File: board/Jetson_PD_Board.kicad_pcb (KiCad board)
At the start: 2 copper layers, 47 parts, among them J1 USB4081-03-A, J2 768250002, Q1 NTTFS5C673NLTAG, Q2 NTTFS5C673NLTAG, Q3 NTTFS5C673NLTAG, U1 APK43070DKZ-13-FA01, U2 USBLC6-2SC6

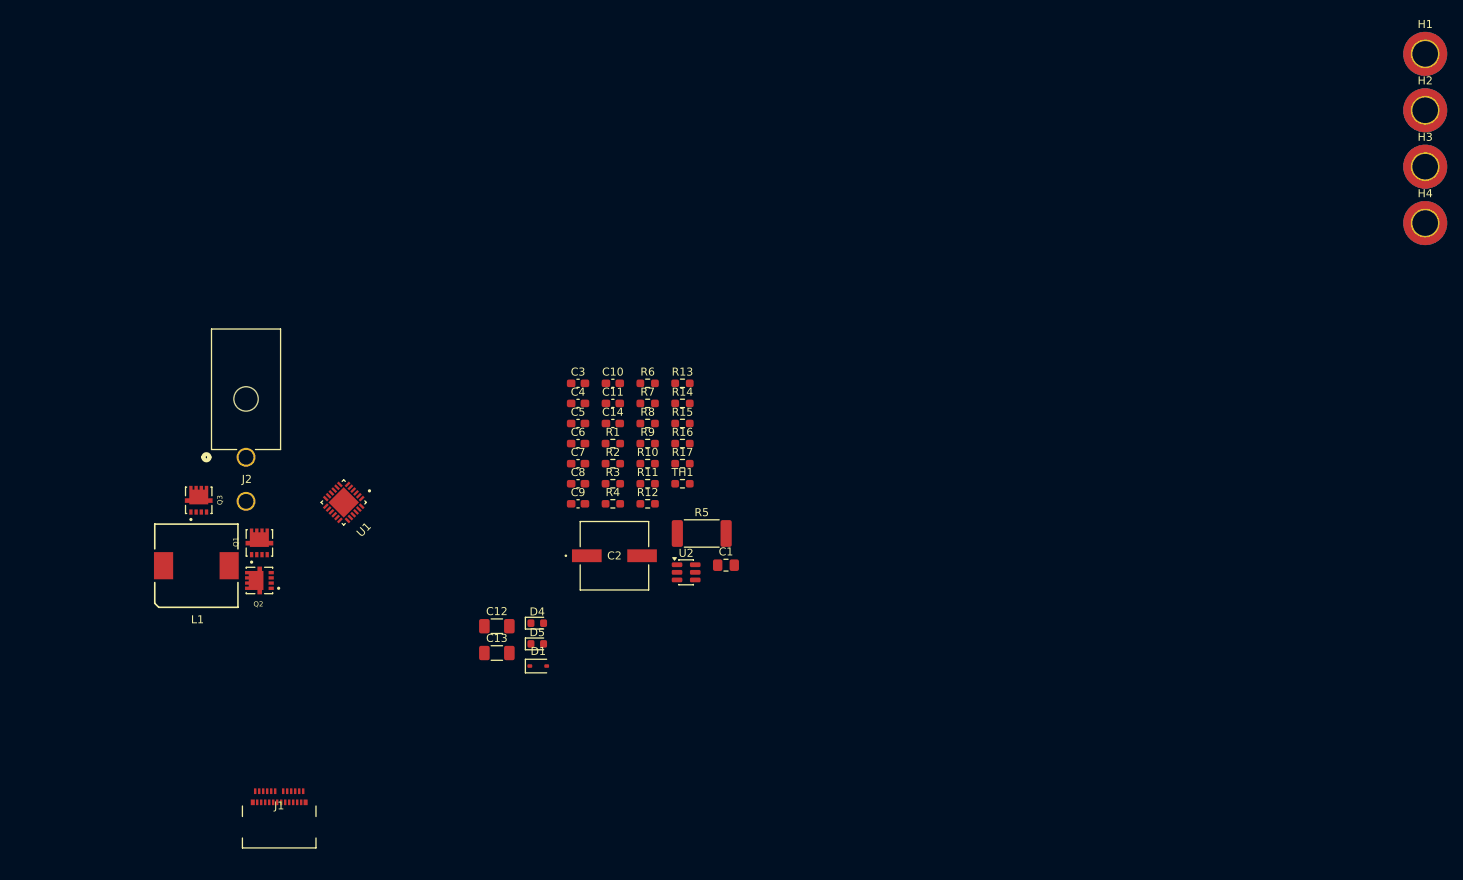
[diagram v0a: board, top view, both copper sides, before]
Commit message: Buck component placement
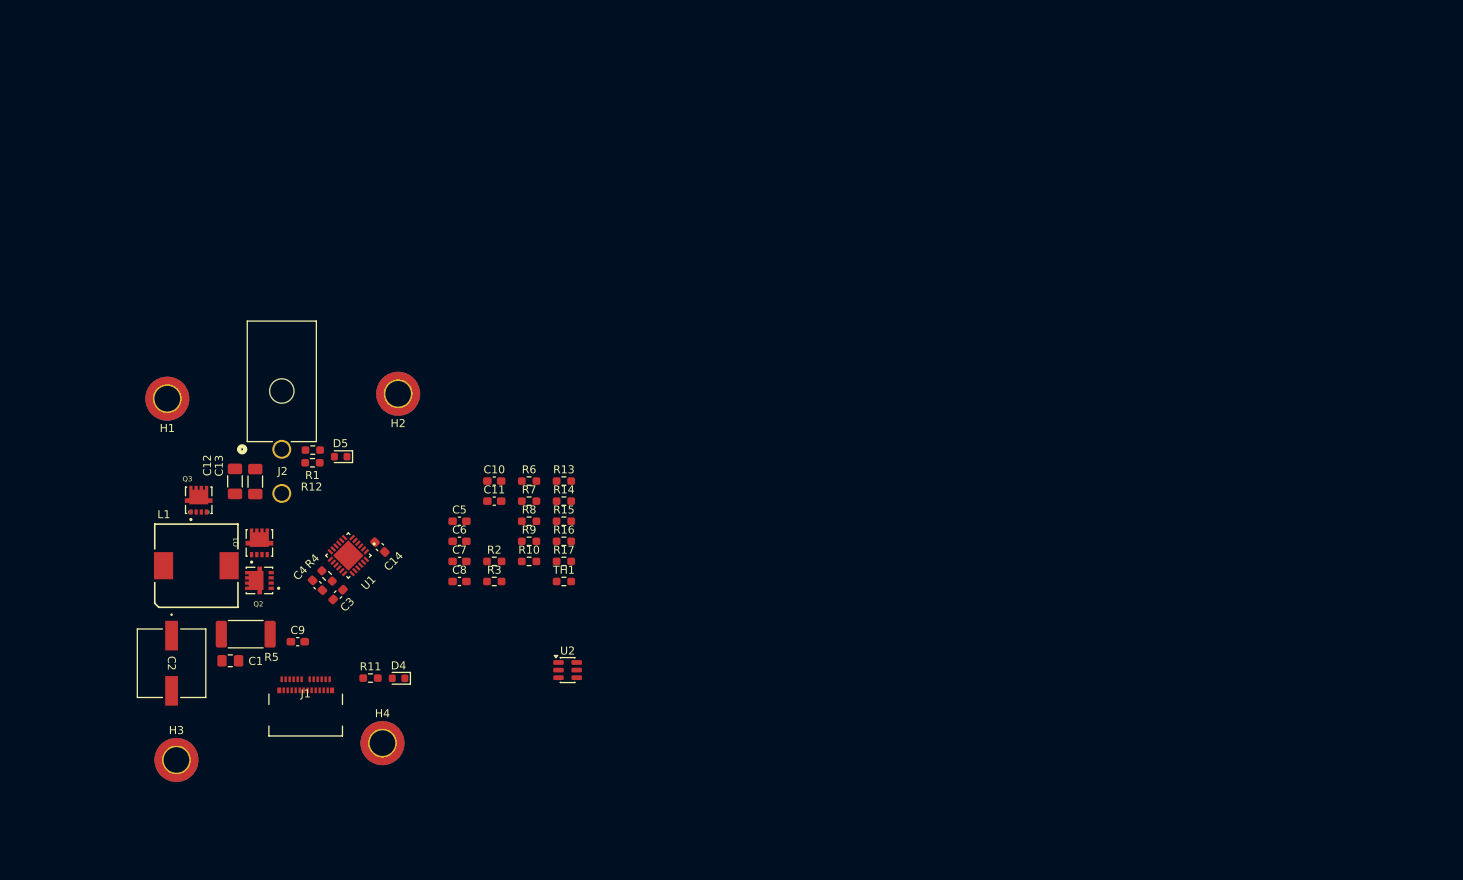
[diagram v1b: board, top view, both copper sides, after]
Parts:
- D1: moved to B.Cu
- moved H3 172.8 mm to (114.7, 118.2)
- moved H1 163.0 mm to (113.5, 73.0), turned to 180 degrees
- moved H4 145.6 mm to (140.4, 116.1)
- moved H2 133.2 mm to (142.4, 72.4), turned to 180 degrees
- moved C1 63.1 mm to (121.4, 105.8)
- moved R5 58.4 mm to (123.3, 102.4)
- moved C2 57.0 mm to (114.0, 106.1), turned to -90 degrees
- moved D1 46.6 mm to (117.4, 87.2), turned to 180 degrees
- moved R11 42.3 mm to (138.9, 107.9)
- moved R12 42.2 mm to (131.7, 81.0)
- moved C3 40.0 mm to (134.9, 97.5), turned to 45 degrees
- moved C4 39.7 mm to (132.3, 96.3), turned to -45 degrees
- moved C9 39.0 mm to (129.8, 103.4)
- moved R1 37.5 mm to (131.7, 79.4)
- moved C12 37.4 mm to (122.0, 83.3), turned to 90 degrees
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
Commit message: Worked on layout
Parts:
- moved R6 33.9 mm to (128.5, 98.5), turned to 90 degrees
- moved R7 31.4 mm to (130.0, 98.5), turned to 90 degrees
- moved R14 29.0 mm to (139.0, 102.0), turned to 90 degrees
- moved R15 28.2 mm to (140.0, 104.5)
- moved C10 27.5 mm to (131.5, 98.5), turned to 90 degrees
- moved R8 27.2 mm to (133.5, 98.6), turned to -90 degrees
- moved U2 23.6 mm to (140.0, 108.0), turned to 180 degrees
- moved R10 21.9 mm to (137.5, 98.6), turned to -90 degrees
- moved R9 21.2 mm to (139.0, 98.6), turned to -90 degrees
- moved R2 20.1 mm to (135.0, 98.6), turned to -90 degrees
- moved C8 15.2 mm to (138.0, 86.5), turned to 90 degrees
- moved C7 15.2 mm to (136.5, 86.5), turned to 90 degrees
- moved R3 14.7 mm to (141.0, 102.0), turned to -90 degrees
- moved C5 13.6 mm to (141.0, 98.5), turned to 90 degrees
- moved C3 12.3 mm to (146.5, 93.5), turned to 0 degrees
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
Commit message: Placed most components
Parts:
- R13: moved to B.Cu
- moved R16 43.5 mm to (123.3, 108.4)
- moved R17 43.1 mm to (123.3, 110.0)
- moved R13 41.3 mm to (122.0, 87.0)
- moved C11 25.4 mm to (130.5, 94.5), turned to 180 degrees
- moved TH1 24.0 mm to (130.5, 93.0), turned to 180 degrees
- moved H4 2.51 mm to (141.3, 118.4)
- moved C3 0.82 mm to (145.8, 93.1)
- moved C4 0.82 mm to (142.3, 94.6)
- moved C6 0.82 mm to (142.3, 91.6)
- moved R4 0.82 mm to (142.3, 93.1)
- moved H2 0.78 mm to (141.7, 72.8)
- moved C7 0.71 mm to (136.0, 87.0)
- moved C8 0.71 mm to (137.5, 87.0)
- moved D4 0.06 mm to (133.4, 106.0)
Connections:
- net Net-(J1-DN2) renamed /USB_DN
- net Net-(J1-DP2) renamed /USB_DP
- net Net-(R14-Pad2) renamed /DP
- net Net-(R15-Pad2) renamed /DN
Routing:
- net /USB_DP: track 0.00 -> 4.25 mm
- net /USB_DN: track 0.00 -> 4.25 mm

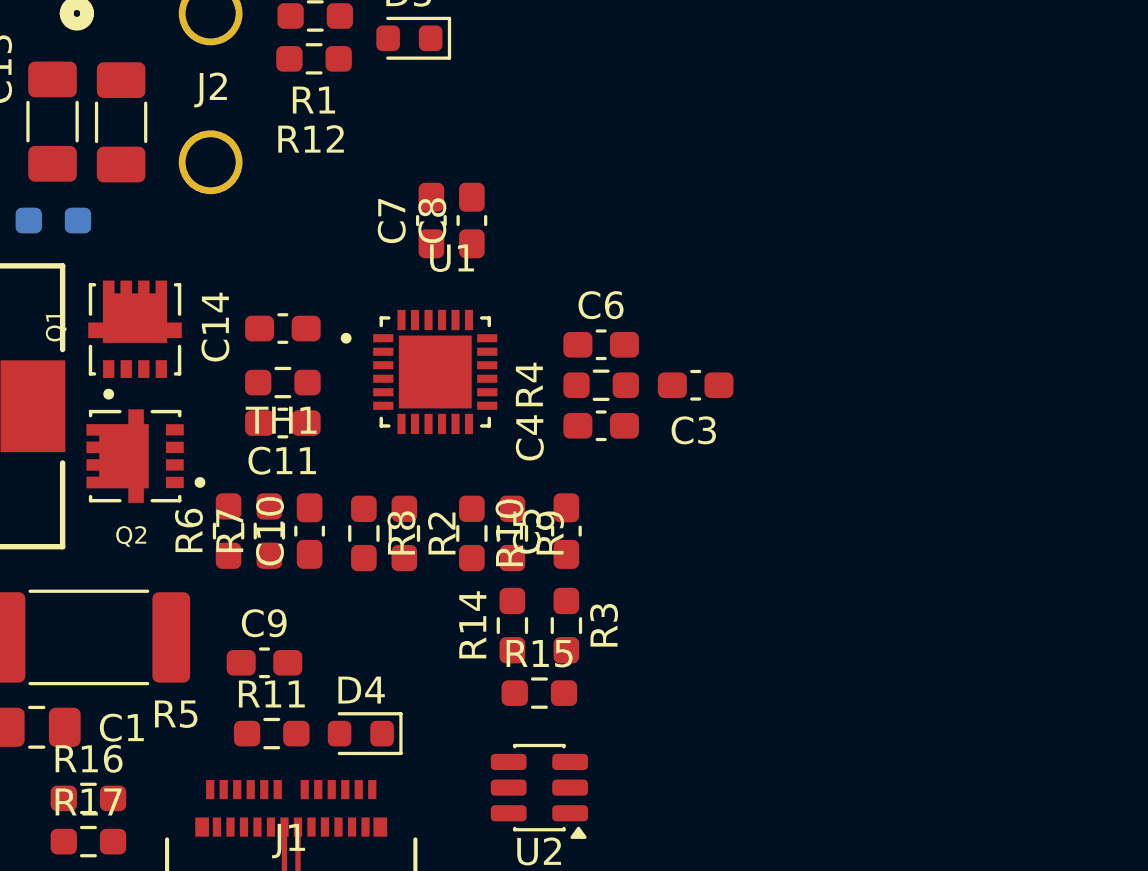
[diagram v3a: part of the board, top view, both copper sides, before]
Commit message: Reviewed first placement and ordered signals on back
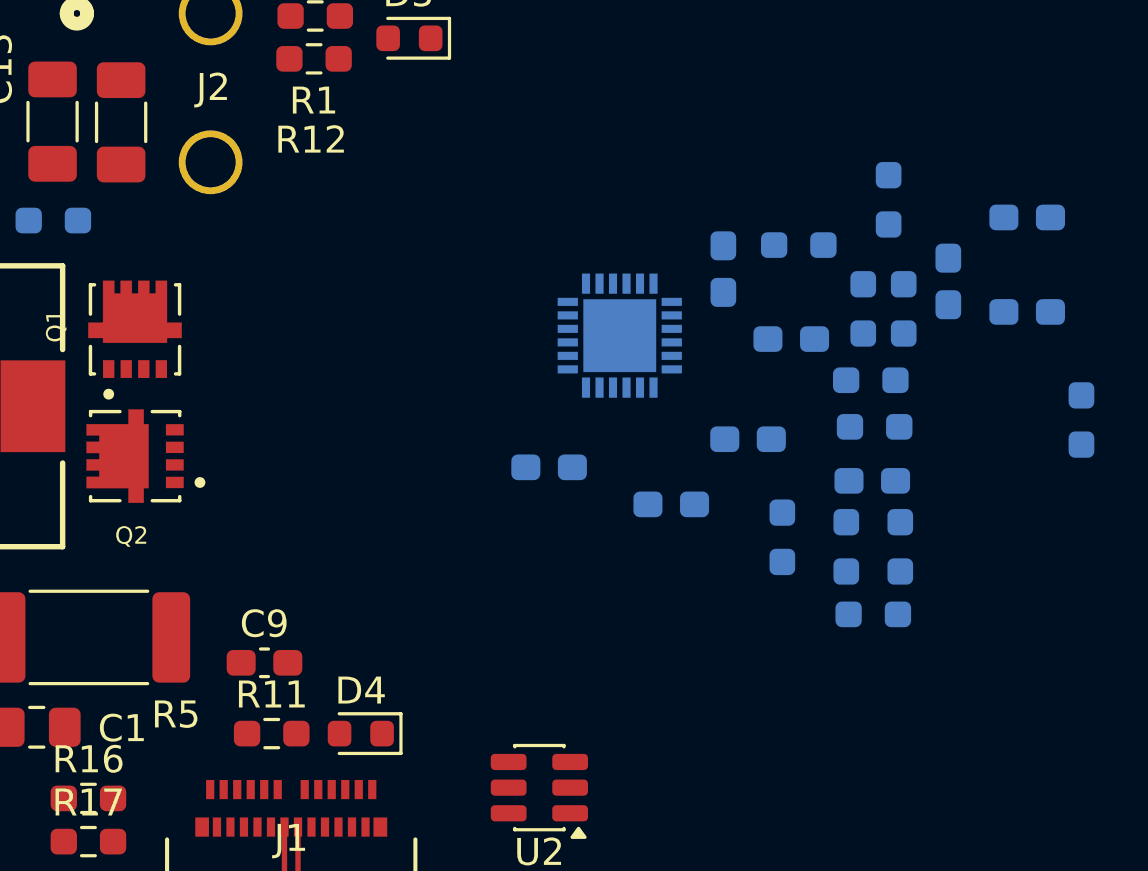
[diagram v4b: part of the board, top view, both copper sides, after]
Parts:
- C10, C11, C14, C3, C4, C5, C6, C7, C8, R10, R14, R15, R2, R3, R4, R6, R7, R8, R9, TH1, U1: moved to B.Cu
- moved R6 31.9 mm to (160.1, 94.4)
- moved C11 27.9 mm to (158.1, 90.4), turned to 0 degrees
- moved C14 27.9 mm to (158.1, 86.9), turned to 0 degrees
- moved TH1 21.8 mm to (152.3, 92.9), turned to 0 degrees
- moved R8 21.7 mm to (153.5, 90.3)
- moved R10 19.8 mm to (152.9, 86.2)
- moved C7 19.3 mm to (155.1, 89.3)
- moved R7 19.0 mm to (149.0, 98.7)
- moved R2 18.9 mm to (152.0, 90.3)
- moved R14 14.7 mm to (153.4, 99.1)
- moved R9 14.0 mm to (152.4, 94.6), turned to 0 degrees
- moved R15 12.7 mm to (152.4, 101.6), turned to 180 degrees
- moved C5 11.5 mm to (152.3, 96.6), turned to 180 degrees
- moved R3 10.8 mm to (151.4, 99.1)
- moved C8 9.48 mm to (146.8, 88.8)
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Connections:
- C7 pad 1: Net-(U1-V5V) -> V5V
- R6 pad 1: V_{out} -> V5V
- R7 pad 1: V_{out} -> V5V
- U1 pad 21: Net-(U1-V5V) -> V5V

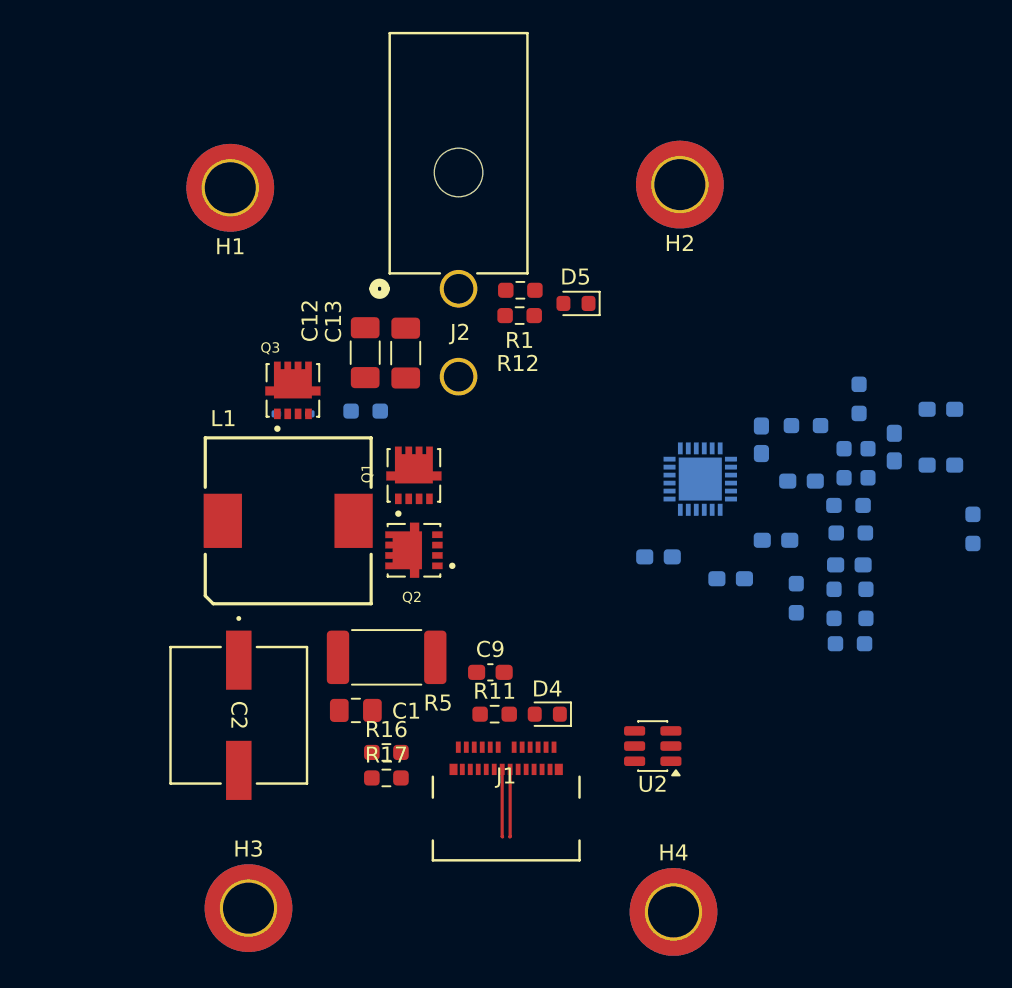
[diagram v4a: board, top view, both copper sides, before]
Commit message: Moved IC and passives in layout
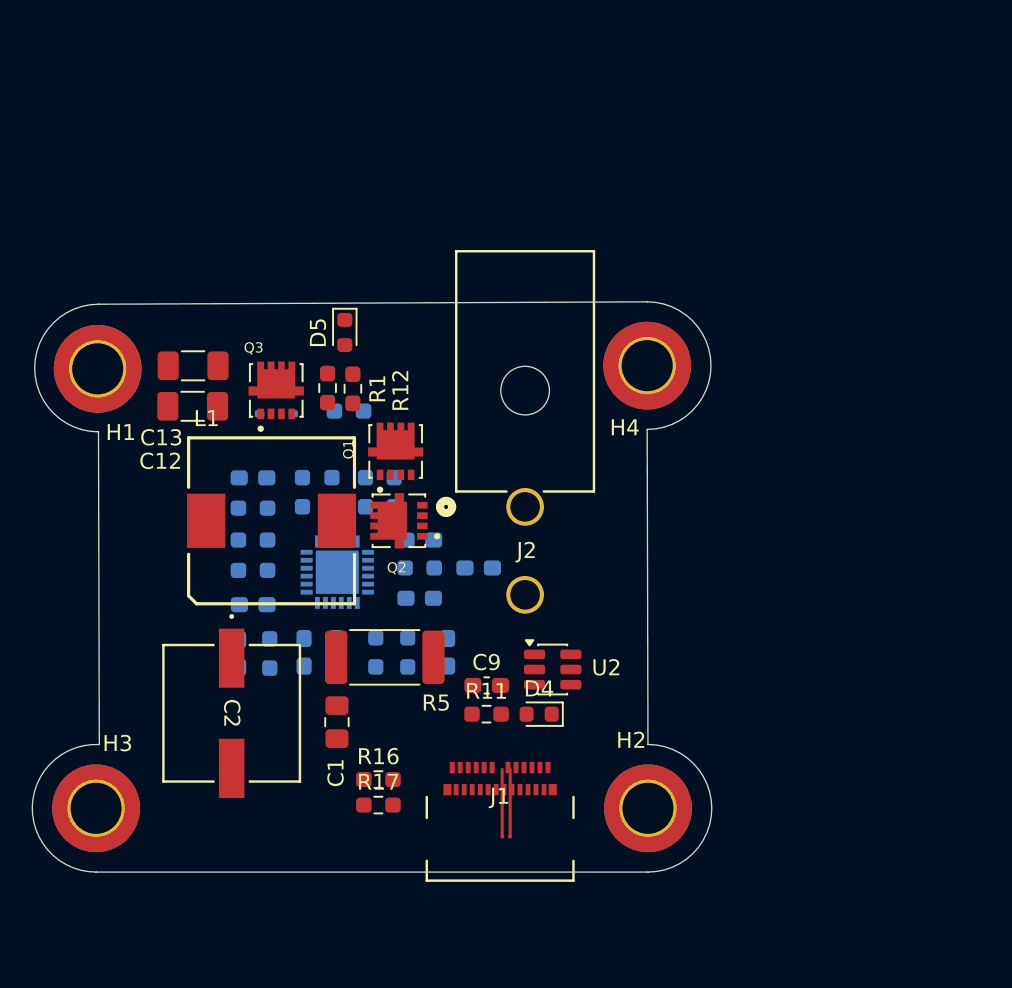
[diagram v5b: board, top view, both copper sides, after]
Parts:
- moved C14 44.8 mm to (114.9, 99.1), turned to 180 degrees
- moved C11 43.1 mm to (114.9, 91.2), turned to 180 degrees
- moved H2 39.2 mm to (139.7, 111.9)
- moved C5 38.7 mm to (114.0, 102.2), turned to 90 degrees
- moved R14 38.6 mm to (114.9, 95.1), turned to 180 degrees
- moved R6 38.2 mm to (122.6, 102.1), turned to -90 degrees
- moved R15 37.7 mm to (114.9, 97.0)
- moved TH1 37.3 mm to (114.9, 93.1), turned to 180 degrees
- moved R3 35.5 mm to (116.0, 102.2), turned to 90 degrees
- moved R8 35.5 mm to (118.0, 92.1), turned to 90 degrees
- moved H4 34.3 mm to (139.7, 84.2)
- moved R2 32.2 mm to (119.9, 92.1), turned to 90 degrees
- moved C7 30.8 mm to (127.1, 102.1), turned to -90 degrees
- moved R9 30.5 mm to (122.0, 92.1), turned to 90 degrees
- moved C8 29.8 mm to (120.1, 102.1), turned to -90 degrees
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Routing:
- net CC2: track 0.00 -> 4.25 mm
- net /USB_DN: track 4.25 -> 0.00 mm
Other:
- board outline added: 42.6 x 35.8 mm

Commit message: Adjusted grid
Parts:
- moved R13 1.62 mm to (122.5, 86.5)
- moved R12 1.30 mm to (122.5, 85.5), turned to -90 degrees
- moved C7 1.14 mm to (126.0, 102.0)
- moved R1 0.89 mm to (120.5, 85.5), turned to -90 degrees
- moved C12 0.70 mm to (111.2, 86.0)
- moved C13 0.66 mm to (111.2, 83.5)
- moved R6 0.65 mm to (122.0, 102.0)
- moved R7 0.65 mm to (124.0, 102.0)
- moved D4 0.50 mm to (132.9, 106.5)
- moved R11 0.50 mm to (129.6, 106.5)
- moved C11 0.47 mm to (114.5, 91.0)
- moved C14 0.47 mm to (114.5, 99.0)
- moved R14 0.45 mm to (114.5, 95.0)
- moved TH1 0.45 mm to (114.5, 93.0)
- moved H2 0.45 mm to (139.5, 111.5)
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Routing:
- net CC2: track 4.25 -> 0.00 mm
- net /USB_DP: track 4.25 -> 0.00 mm
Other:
- board size 42.6 x 35.8 mm -> 41.5 x 34.5 mm
